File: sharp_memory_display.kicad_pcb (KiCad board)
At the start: 2 copper layers, 34.2 x 20 mm, 18 parts, among them J1 Conn_01x05, J2 Conn_01x10, J3 Conn_01x05_Male

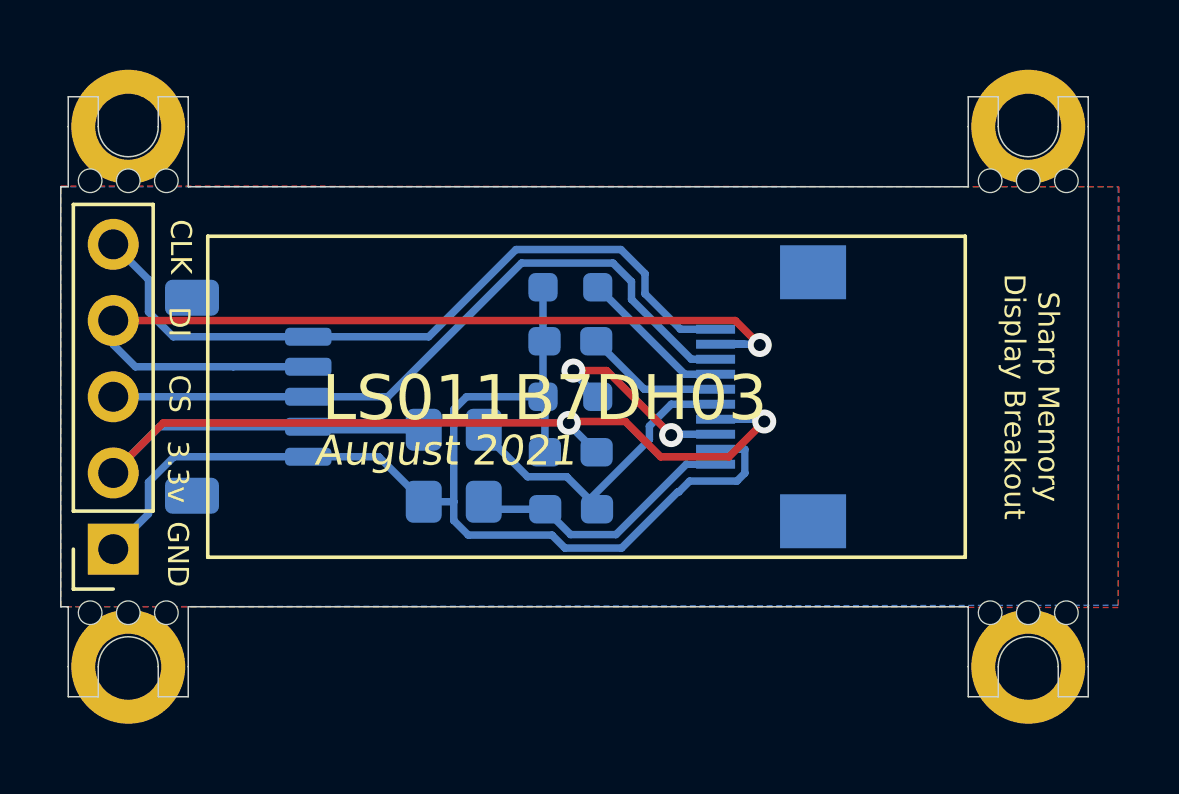
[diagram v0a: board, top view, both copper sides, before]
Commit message: add solderable pad
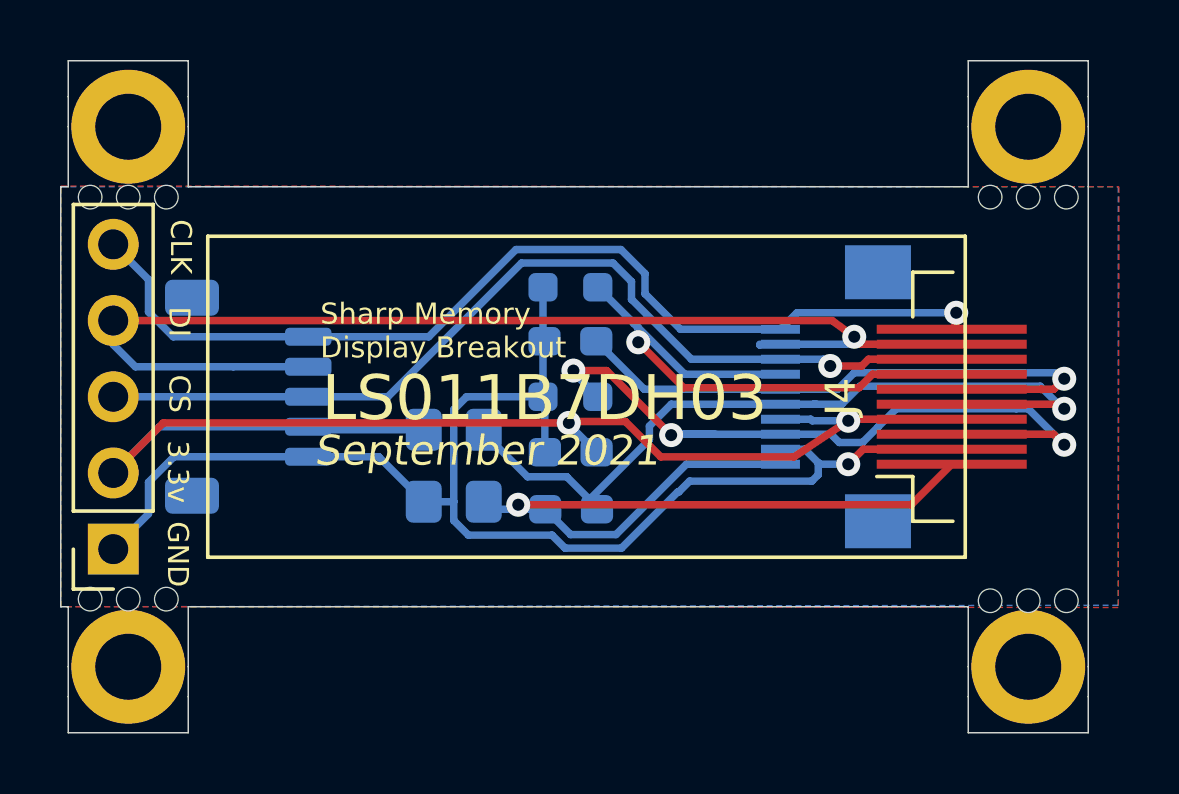
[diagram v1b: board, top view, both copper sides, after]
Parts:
- removed the REF** at (54.8, 23.5)
- removed the REF** at (24.8, 37.4)
- removed the REF** at (24.8, 23.5)
- removed the REF** at (54.8, 37.4)
- added J4: Conn_01x10, Connector_FFC-FPC:Hirose_FH12-10S-0.5SH_1x10-1MP_P0.50mm_Horizontal, F.Cu at (52.2, 30.5)
- added REF**: breakaway-mousebites-three, Keebio-Parts:breakaway-mousebites-three, F.Cu at (54.8, 24.1)
- added REF**: breakaway-mousebites-three, Keebio-Parts:breakaway-mousebites-three, F.Cu at (24.8, 37.5)
- added REF**: breakaway-mousebites-three, Keebio-Parts:breakaway-mousebites-three, F.Cu at (24.8, 24.1)
- added REF**: breakaway-mousebites-three, Keebio-Parts:breakaway-mousebites-three, F.Cu at (54.8, 37.5)
- moved J2 2.16 mm to (52.9, 30.5)
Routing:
- net EXTMODE: track 6.85 -> 24.9 mm, vias 2 -> 3
- net VSSA: track 9.15 -> 26.6 mm, vias 0 -> 1
- net VDDA: track 10.8 -> 27.1 mm, vias 0 -> 1
- net DISP: track 4.64 -> 20.5 mm, vias 0 -> 1
- net EXTCOMIN: track 5.13 -> 19.3 mm, vias 0 -> 1
- net SCLK: track 24.7 -> 33.5 mm, vias 0 -> 1
- net SCS: track 23.6 -> 31.7 mm, vias 0 -> 1
- net VSS: track 39.2 -> 46.3 mm, vias 0 -> 1
- net VDD: track 37.4 -> 44.3 mm
- net SI: track 32.0 -> 38.7 mm
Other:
- board size 34.2 x 20 mm -> 34.2 x 22.4 mm
- board text added: "September 2021"
- board text removed: "August 2021"

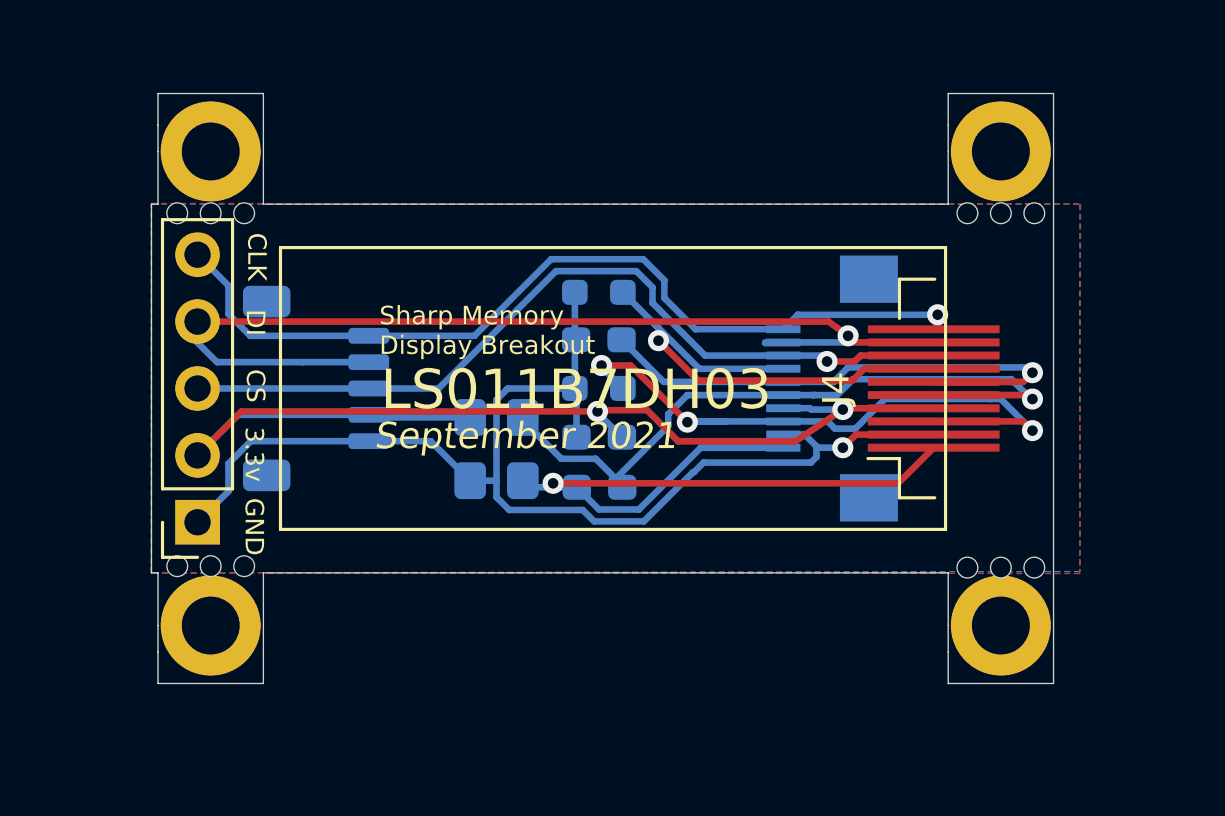
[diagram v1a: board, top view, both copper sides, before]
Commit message: add pullup resistor for DISP
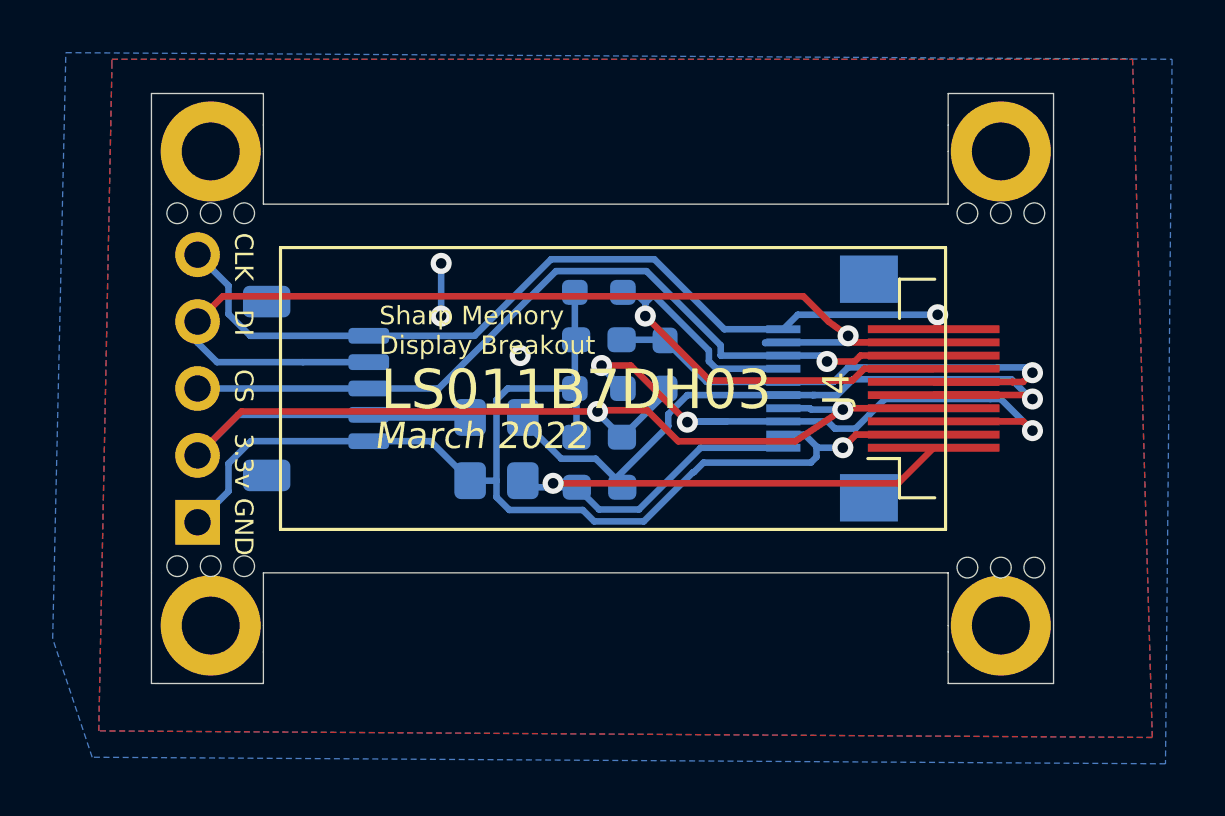
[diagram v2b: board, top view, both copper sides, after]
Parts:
- added R3: 10k, Resistor_SMD:R_0603_1608Metric_Pad0.98x0.95mm_HandSolder, B.Cu at (42.0, 29.6)
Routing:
- net VDD: track 44.3 -> 46.8 mm
- net VSS: track 46.3 -> 48.3 mm, vias 1 -> 4
- net EXTCOMIN: track 19.3 -> 21.2 mm
- net SI: track 38.7 -> 39.5 mm
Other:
- outline, holes or cut-outs redrawn
- board text added: "March 2022"
- board text removed: "September 2021"

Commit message: add 3d files and update readme
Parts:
- removed J4: Conn_01x10, Connector_FFC-FPC:Hirose_FH12-10S-0.5SH_1x10-1MP_P0.50mm_Horizontal
- moved FB1 63.6 mm to (80.2, 77.0)
- moved FB2 63.5 mm to (80.2, 79.3)
- moved C2 63.2 mm to (83.2, 79.9), turned to -90 degrees
- moved H1 63.1 mm to (95.4, 87.7)
- moved H4 63.1 mm to (95.4, 69.7)
- moved REF** 63.1 mm to (95.4, 85.7)
- moved R2 62.9 mm to (80.0, 75.0)
- moved REF** 62.6 mm to (95.4, 71.7), turned to 180 degrees
- moved J3 62.6 mm to (68.7, 78.7)
- moved R1 62.6 mm to (76.1, 81.3)
- moved C1 62.5 mm to (77.0, 78.6), turned to -90 degrees
- moved J1 62.3 mm to (63.6, 83.8)
- moved H2 62.1 mm to (63.9, 69.7)
- moved H3 62.1 mm to (63.9, 87.7)
- moved REF** 62.1 mm to (63.9, 85.7)
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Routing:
- net VDDA: track 27.1 -> 6.54 mm, vias 1 -> 0
- net VSSA: track 26.6 -> 6.80 mm, vias 1 -> 0
- net VDD: track 46.8 -> 29.2 mm, vias 2 -> 0
- net EXTCOMIN: track 21.2 -> 7.19 mm, vias 1 -> 0
- net SI: track 39.5 -> 27.7 mm, vias 1 -> 0
- net EXTMODE: track 24.9 -> 14.8 mm, vias 3 -> 0
- net DISP: track 20.5 -> 12.8 mm, vias 1 -> 0
- net SCLK: track 33.2 -> 28.1 mm, vias 1 -> 0
- net SCS: track 31.5 -> 27.3 mm, vias 1 -> 0
- net VSS: track 48.3 -> 50.2 mm, vias 4 -> 1
- removed copper zone on B.Cu, net VSS
- removed copper zone on F.Cu, net VSS
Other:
- board size 34.2 x 22.4 mm -> 35.5 x 22 mm
- board text added: "27 August 2022"
- board text added: "CLK DI CS 3V3 GND"
- board text added: "LS011B7DH03 Sharp Memory Display Breakout"
- board text added: "https://github.com/karnadii/ sharp_memory_display_breakout"
- board text removed: "3.3V"
- board text removed: "3.3v"
- board text removed: "CLK"
- board text removed: "CS"
- board text removed: "DI"
- board text removed: "GND"
- board text removed: "LS011B7DH03"
- board text removed: "MOSI"
- board text removed: "March 2022"
- board text removed: "SCLK"
- board text removed: "SCS"
- board text removed: "Sharp Memory Display Breakout"

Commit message: nice!view compatible
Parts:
- removed R1, R2, R3: 10k, Resistor_SMD:R_0603_1608Metric_Pad0.98x0.95mm_HandSolder
- moved REF** 0.10 mm to (63.8, 85.7)
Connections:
- C1 pad 2: VSS -> EXTCOMIN
- C3 pad 1: VDD -> DISP
- C3 pad 2: VSS -> EXTCOMIN
- FB1 pad 2: VDD -> DISP
- FB2 pad 1: VSS -> EXTCOMIN
- J1 pad 1: VSS -> SCS
- J1 pad 2: VDD -> EXTCOMIN
- J1 pad 3: SCS -> DISP
- J1 pad 4: SI -> SCLK
- J1 pad 5: SCLK -> SI
- J2 pad 7: VDD -> DISP
- J2 pad 8: EXTMODE -> EXTCOMIN
- J2 pad 9: VSS -> EXTCOMIN
- J3 pad 1: VSS -> SCS
- J3 pad 2: VDD -> EXTCOMIN
- J3 pad 3: SCS -> DISP
- J3 pad 4: SI -> SCLK
- J3 pad 5: SCLK -> SI
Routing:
- net VSS: track 50.2 -> 0.00 mm, vias 1 -> 0
- net VDD: track 29.2 -> 0.00 mm
- net EXTCOMIN: track 7.19 -> 34.5 mm
- net DISP: track 12.8 -> 35.0 mm
- net EXTMODE: track 14.8 -> 0.00 mm
- net SCS: track 27.3 -> 32.0 mm
- net SCLK: track 28.1 -> 25.2 mm
- net SI: track 27.7 -> 28.7 mm
- net VSSA: track 6.80 -> 6.11 mm
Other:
- board text added: "10 October 2022"
- board text added: "MOSI SCK 3v3 GND CS"
- board text removed: "27 August 2022"
- board text removed: "CLK DI CS 3V3 GND"

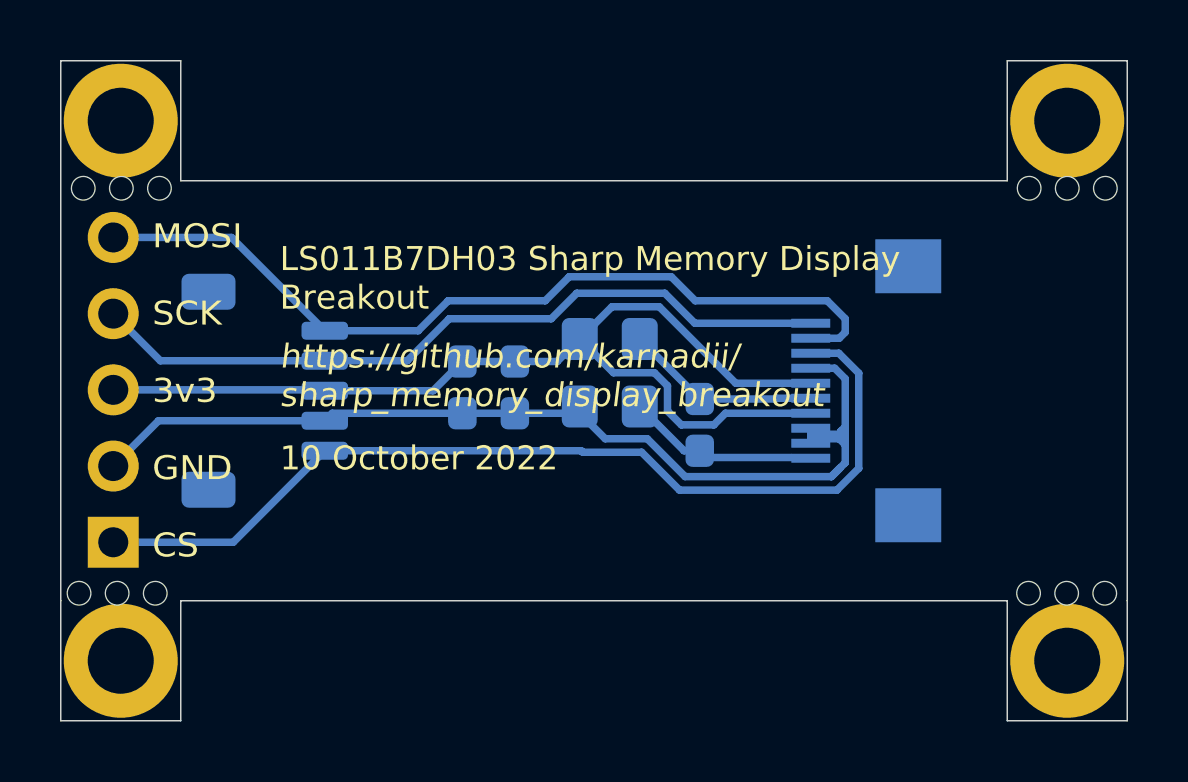
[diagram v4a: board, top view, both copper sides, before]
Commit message: no mounting holes version
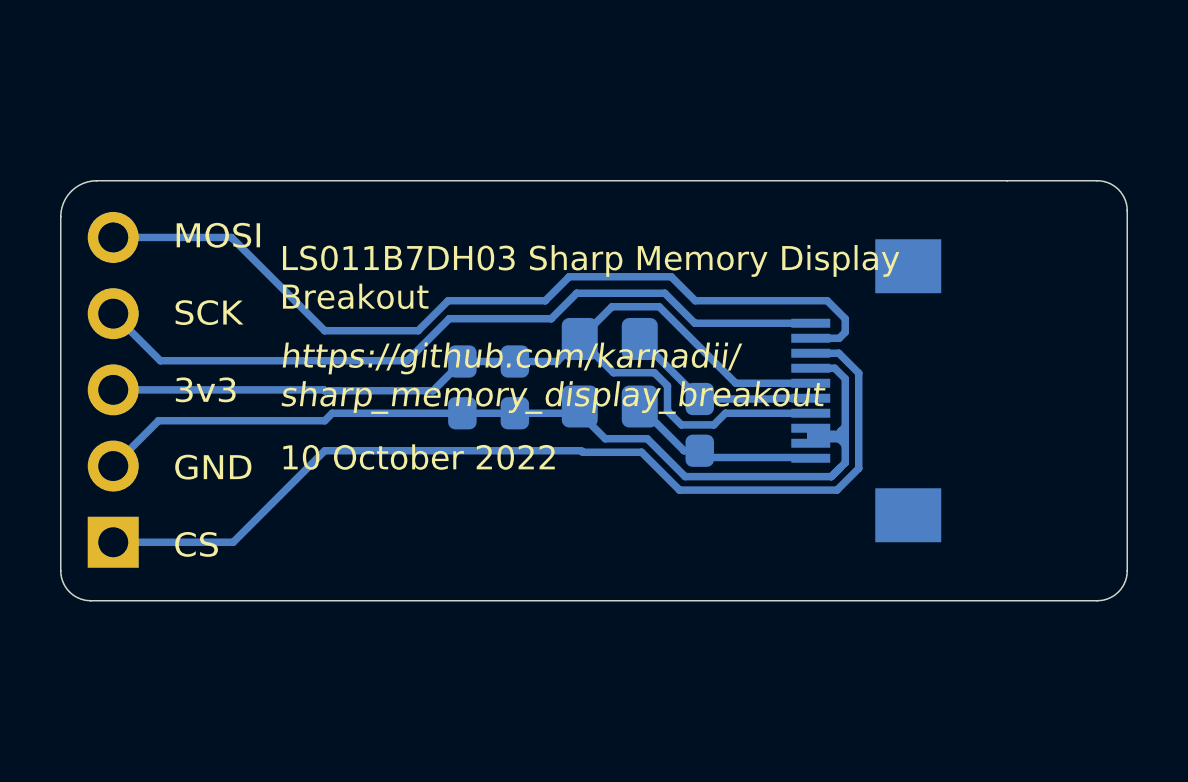
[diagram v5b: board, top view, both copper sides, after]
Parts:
- removed H1, H2, H3, H4: MountingHole, MountingHole:MountingHole_2.2mm_M2_DIN965_Pad
- removed J3: Conn_01x05_Male, Connector_JST:JST_SH_SM05B-SRSS-TB_1x05-1MP_P1.00mm_Horizontal
- removed REF** (x4): breakaway-mousebites-three, Keebio-Parts:breakaway-mousebites-three
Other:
- board size 35.5 x 22 mm -> 35.5 x 14 mm
